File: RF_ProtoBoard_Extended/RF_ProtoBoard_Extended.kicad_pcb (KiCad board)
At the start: 2 copper layers, 99.6 x 87.6 mm, 12 parts, among them J1 Screw_Terminal_01x02, J2 Conn_VPlus_Gnd

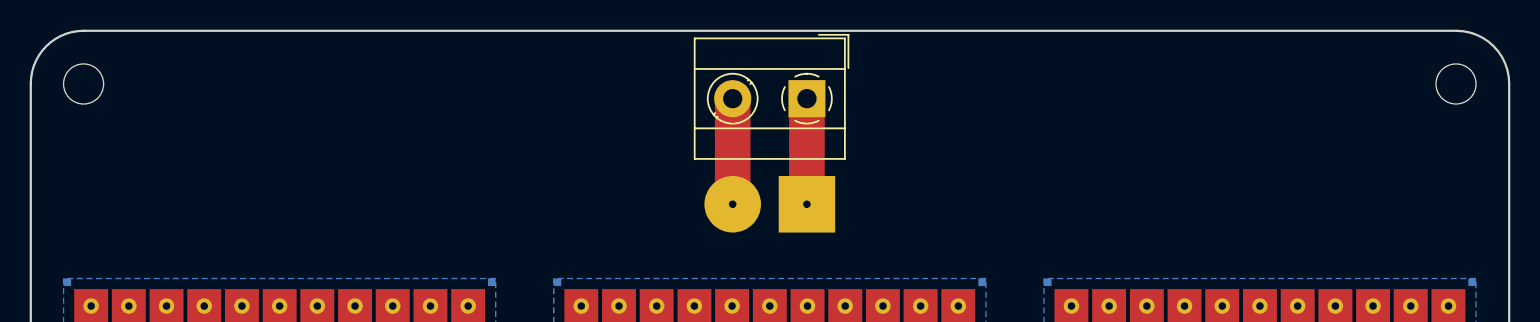
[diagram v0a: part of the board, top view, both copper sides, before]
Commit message: Basic update.
Did basic power update. Would like to add an SOIC-8 or such of parts I normally use.
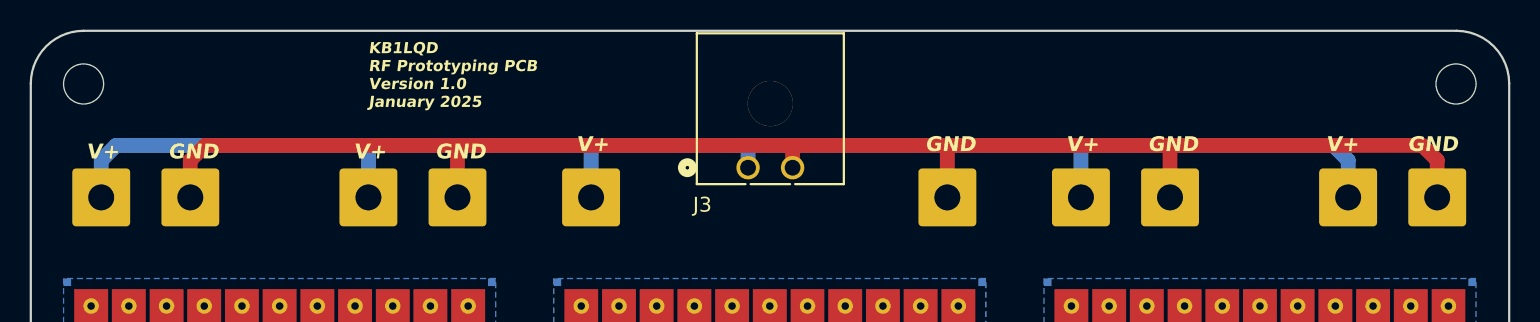
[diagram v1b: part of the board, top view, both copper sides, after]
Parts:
- added J10: Conn_01x01_Pin, Connector_Wire:SolderWire-1sqmm_1x01_D1.4mm_OD3.9mm, F.Cu at (111.0, 13.0)
- added J11: Conn_01x01_Pin, Connector_Wire:SolderWire-1sqmm_1x01_D1.4mm_OD3.9mm, F.Cu at (93.0, 13.0)
- added J12: Conn_01x01_Pin, Connector_Wire:SolderWire-1sqmm_1x01_D1.4mm_OD3.9mm, F.Cu at (78.0, 13.0)
- added J3: Conn_01x02_Pin, RF_ProtoBoard:CONN_SD-43650-001_02_MOL, F.Cu at (64.6, 11.0)
- added J4: Conn_01x01_Pin, Connector_Wire:SolderWire-1sqmm_1x01_D1.4mm_OD3.9mm, F.Cu at (105.0, 13.0)
- added J5: Conn_01x01_Pin, Connector_Wire:SolderWire-1sqmm_1x01_D1.4mm_OD3.9mm, F.Cu at (87.0, 13.0)
- added J6: Conn_01x01_Pin, Connector_Wire:SolderWire-1sqmm_1x01_D1.4mm_OD3.9mm, F.Cu at (54.0, 13.0)
- added J8: Conn_01x01_Pin, Connector_Wire:SolderWire-1sqmm_1x01_D1.4mm_OD3.9mm, F.Cu at (27.0, 13.0)
- added J9: Conn_01x01_Pin, Connector_Wire:SolderWire-1sqmm_1x01_D1.4mm_OD3.9mm, F.Cu at (45.0, 13.0)
- A1, A2, A3, A4, A5, A6: value (none) -> GndRing_RF_ProtoBoard_Module
- J1: value Screw_Terminal_01x02 -> Conn_01x01_Pin; footprint TerminalBlock_MetzConnect:TerminalBlock_MetzConnect_Type055_RT01502HDWU_1x02_P5.00mm_Horizontal -> Connector_Wire:SolderWire-1sqmm_1x01_D1.4mm_OD3.9mm
- J2: value Conn_VPlus_Gnd -> Conn_01x01_Pin; footprint RF_ProtoBoard:VPlus_Gnd_Pads -> Connector_Wire:SolderWire-1sqmm_1x01_D1.4mm_OD3.9mm
- moved J1 48.0 mm to (21.0, 13.0), turned to 0 degrees
- moved J2 27.0 mm to (39.0, 13.0)
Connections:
- J1 pad 1: /Gnd -> /V+
- J2 pad 1: /Gnd -> /V+
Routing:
- net /V+: track 7.11 -> 103.3 mm
- net /Gnd: track 7.11 -> 101.9 mm
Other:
- board text added: "GND"
- board text added: "KB1LQD RF Prototyping PCB Version 1.0 January 2025"
- board text added: "V+"

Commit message: Ready to output.
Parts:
- H1, H2, H3, H4: footprint RF_ProtoBoard:MountingHole_2.7mm_M2.5_Clearance_1.7mm -> MountingHole:MountingHole_3.2mm_M3
- J1, J10, J11, J12, J2, J4, J5, J6, J8, J9: footprint Connector_Wire:SolderWire-1sqmm_1x01_D1.4mm_OD3.9mm -> Connector_Wire:SolderWire-0.75sqmm_1x01_D1.25mm_OD2.3mm

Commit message: Ordered.
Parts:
- moved A1 90.5 mm to (109.2, 81.8)
- moved A3 90.5 mm to (175.2, 81.8)
- moved A4 90.5 mm to (109.2, 114.9)
- moved A6 90.5 mm to (175.2, 114.9)
- moved H1 90.5 mm to (96.0, 54.2)
- moved H2 90.5 mm to (188.4, 54.2)
- moved H3 90.5 mm to (96.0, 134.6)
- moved H4 90.5 mm to (188.4, 134.7)
- moved J1 90.5 mm to (97.2, 61.8)
- moved J10 90.5 mm to (187.2, 61.8)
- moved J11 90.5 mm to (169.2, 61.8)
- moved J12 90.5 mm to (154.2, 61.8)
- moved J2 90.5 mm to (115.2, 61.8)
- moved J4 90.5 mm to (181.2, 61.8)
- moved J5 90.5 mm to (163.2, 61.8)
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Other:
- board text removed: "${ProductNumberPlaceholder}"
- board text removed: "${REVISION}"
